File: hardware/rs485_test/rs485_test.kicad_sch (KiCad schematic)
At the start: 0 parts

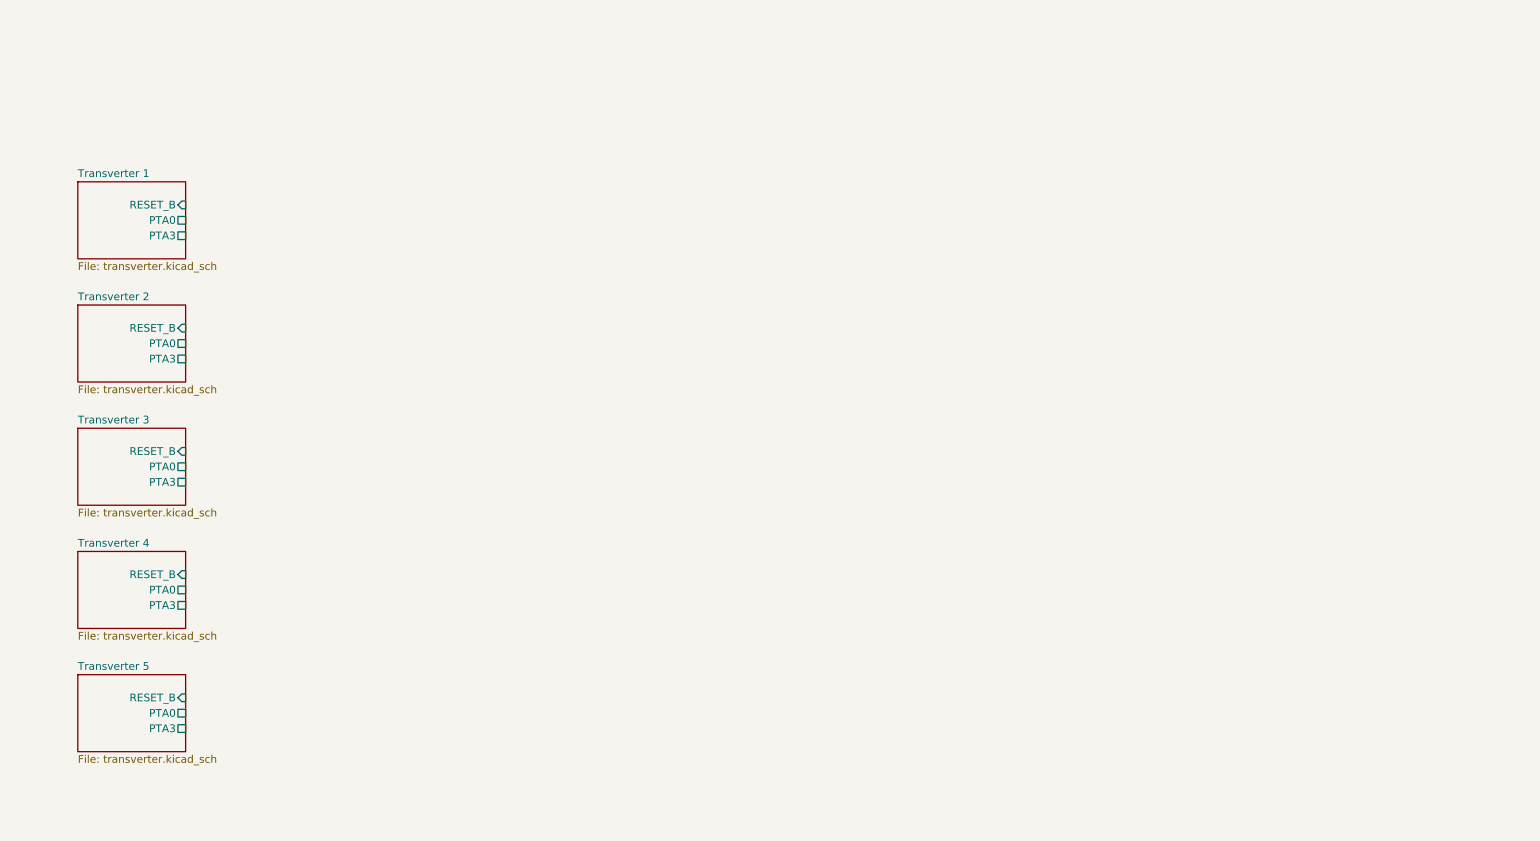
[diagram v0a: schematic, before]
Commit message: Added RS485 driver and AXI GPIO for read/write
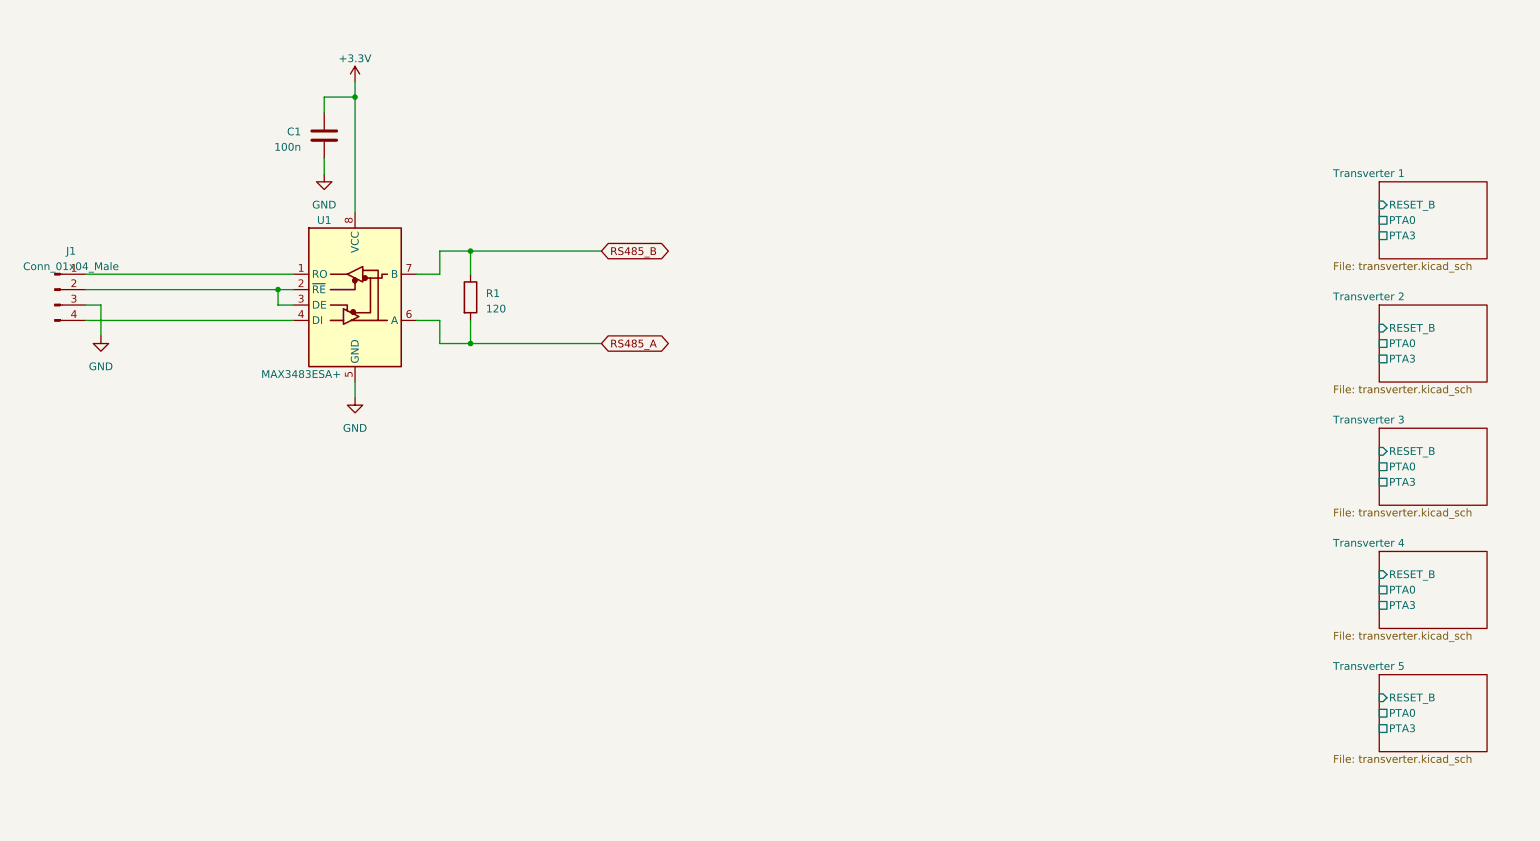
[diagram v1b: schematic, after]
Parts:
- added C1: 100n, Capacitor_SMD:C_0402_1005Metric, symbol Device:C
- added J1: Conn_01x04_Male, Connector_PinHeader_2.54mm:PinHeader_1x04_P2.54mm_Vertical, symbol Connector:Conn_01x04_Male
- added R1: 120, Resistor_SMD:R_0603_1608Metric, symbol Device:R
- added U1: MAX3483ESA+, Package_SO:SO-8_3.9x4.9mm_P1.27mm, symbol Interface_UART:MAX3483
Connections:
- new net: J1.1 (Pin_1), U1.1 (RO)
- new net: J1.2 (Pin_2), U1.2 (~RE), U1.3 (DE)
- new net: J1.4 (Pin_4), U1.4 (DI)
- new net +3V3: C1.1, U1.8 (VCC)
- new net GND: C1.2, J1.3 (Pin_3), U1.5 (GND)
- new net RS485_A: R1.2, U1.6 (A)
- new net RS485_B: R1.1, U1.7 (B)

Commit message: Added RS485 test board
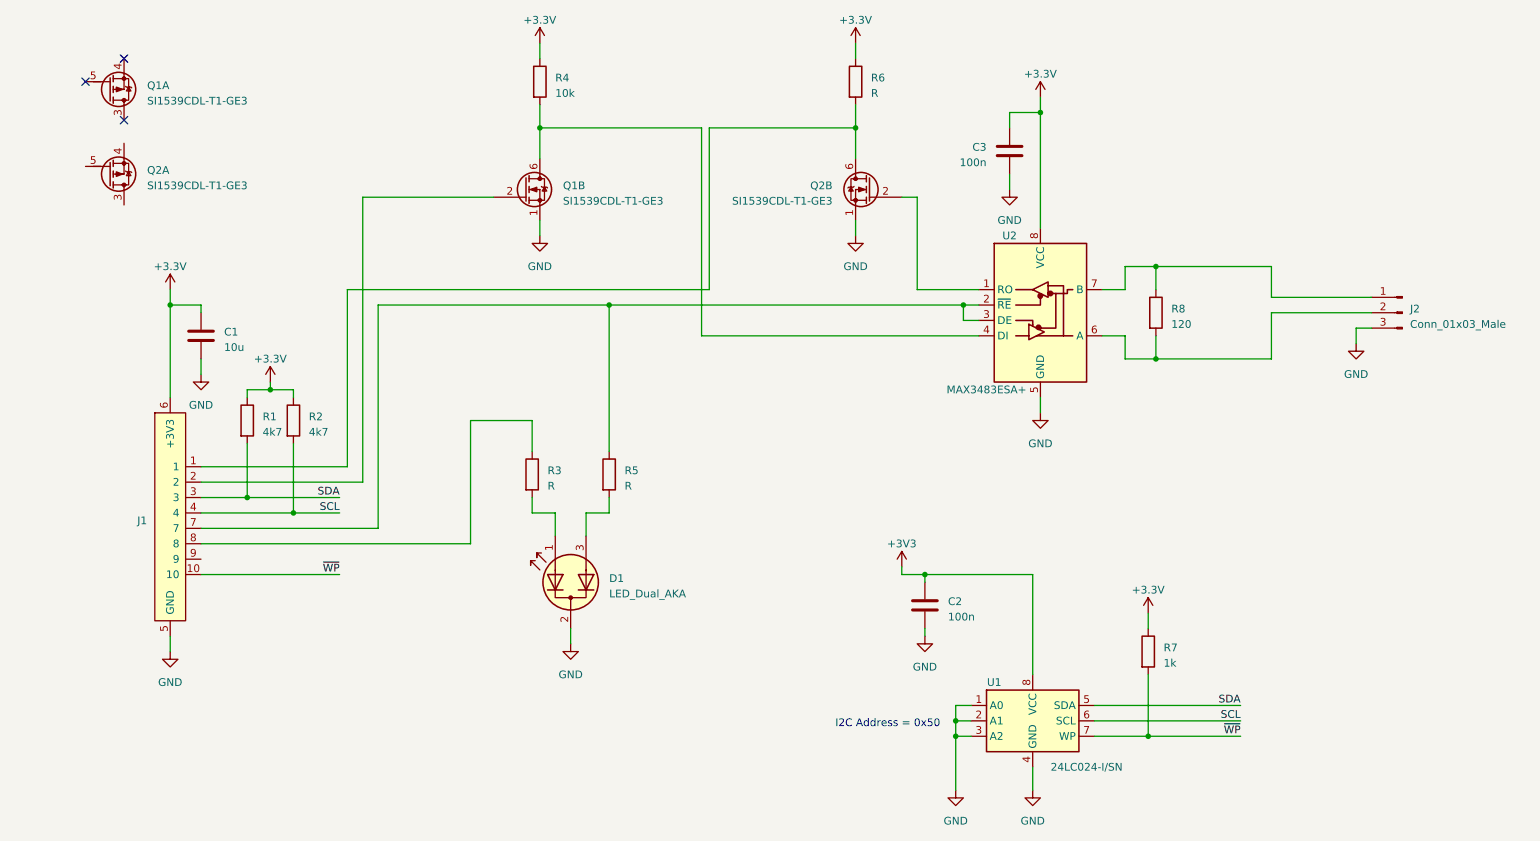
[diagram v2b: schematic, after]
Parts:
- removed J1: Conn_01x04_Male, Connector_PinHeader_2.54mm:PinHeader_1x04_P2.54mm_Vertical, symbol Connector:Conn_01x04_Male
- added C1: 10u, Capacitor_SMD:C_0603_1608Metric, symbol Device:C
- added C2: 100n, Capacitor_SMD:C_0402_1005Metric, symbol Device:C
- added D1: LED_Dual_AKA, LED_THT:LED_D5.0mm-3, symbol Device:LED_Dual_AKA
- added J1: Connector_PMOD_2x6_Peripheral, Connector_WUT:PMOD_Wurth_61301221021_Horizontal, symbol Connector_WUT:Connector_PMOD_2x6_Peripheral
- added J2: Conn_01x03_Male, Connector_JST:JST_PH_B3B-PH-K_1x03_P2.00mm_Vertical, symbol Connector:Conn_01x03_Male
- added Q1, Q2: SI1539CDL-T1-GE3, Package_TO_SOT_SMD:SOT-363_SC-70-6, symbol FET_WUT:SI1539CDL-T1-GE3
- added R1, R2: 4k7, Resistor_SMD:R_0603_1608Metric, symbol Device:R
- added R3, R5, R6: R, Resistor_SMD:R_0603_1608Metric, symbol Device:R
- added R4: 10k, Resistor_SMD:R_0603_1608Metric, symbol Device:R
- added R7: 1k, Resistor_SMD:R_0603_1608Metric, symbol Device:R
- added U1: 24LC024-I/SN, Package_SO:SO-8_3.9x4.9mm_P1.27mm, symbol Memory_EEPROM:24LC02
- renumbered C1 to C3, R1 to R8, U1 to U2
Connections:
- net +3V3: now also C1.1, C2.1, J1.12 (+3V3), J1.6 (+3V3), R1.1, R2.1, R4.1, R6.1, R7.1, U1.8 (VCC)
- net GND: now also C1.2, C2.2, D1.2 (K), J1.11 (GND), J1.5 (GND), J2.3 (Pin_3), Q1.1, Q2.1, U1.1 (A0), U1.2 (A1), U1.3 (A2), U1.4 (GND)
- net at U2.1 (RO): now also Q2.2
- net at U2.2 (~RE), U2.3 (DE): now also J1.7, R5.1
- net at U2.4 (DI): now also Q1.6, R4.2
- net RS485_A: no longer names the net of R8.2, U2.6 (A)
- net RS485_A: now also J2.2 (Pin_2)
- net RS485_B: no longer names the net of R8.1, U2.7 (B)
- net RS485_B: now also J2.1 (Pin_1)
- new net: D1.1 (A1), R3.2
- new net: D1.3 (A2), R5.2
- new net: J1.1, Q2.6, R6.2
- new net: J1.8, R3.1
- new net: J1.2, Q1.2
- new net SCL: J1.4, R2.2, U1.6 (SCL)
- new net SDA: J1.3, R1.2, U1.5 (SDA)
- new net ~WP: J1.10, R7.2, U1.7 (WP)
- no-connect marks 0 -> 3
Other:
- removed sheet Transverter 1
- removed sheet Transverter 2
- removed sheet Transverter 3
- removed sheet Transverter 4
- removed sheet Transverter 5
- note added: "I2C Address = 0x50"
- moved on the sheet: C3, R8, U2
